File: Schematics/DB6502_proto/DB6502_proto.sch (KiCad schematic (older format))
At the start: 27 parts, among them SW1 Reset, U1 DS1813, U10 62256, U11 74AC138, U12 28C256, U13 22V10C, U2 74AC32, U3 74HC21, U4 65C02S, U5 74AC74, U6 74HC74, U7 74AC04, U8 62256, U9 74AC08, X1 14MHz

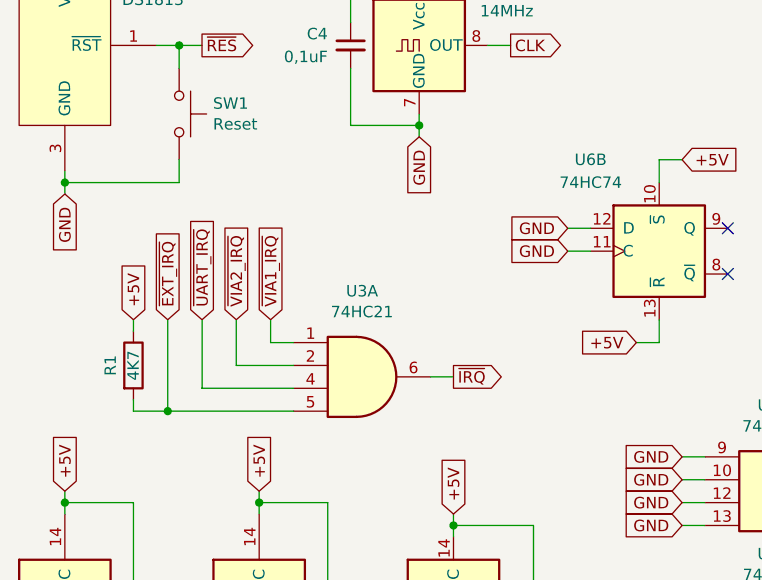
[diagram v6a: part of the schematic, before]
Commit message: Added missing pull-up on UART IRQ line
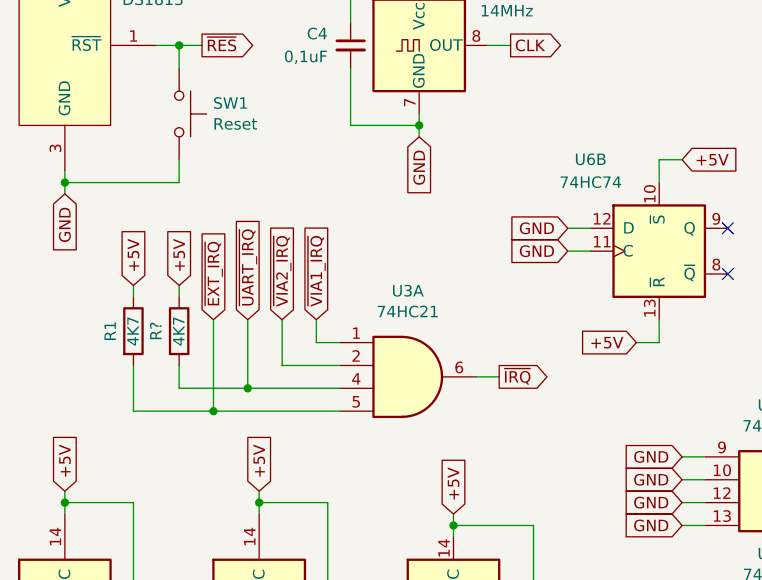
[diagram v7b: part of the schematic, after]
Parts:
- added R?: 4K7, symbol Device:R
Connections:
- net +5V: now also R?.1
- net ~UART_IRQ: now also R?.2
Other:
- moved on the sheet: R1, U3A
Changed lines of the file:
@@
 L 74xx:74LS21 U3
 U 1 1 5FB20233
-P 2150 5800
-F 0 "U3" H 2150 6175 50  0000 C CNN
-F 1 "74HC21" H 2150 6084 50  0000 C CNN
-F 2 "" H 2150 5800 50  0001 C CNN
-F 3 "http://www.ti.com/lit/gpn/sn74LS21" H 2150 5800 50  0001 C CNN
-	1    2150 5800
+P 2350 5800
+F 0 "U3" H 2350 6175 50  0000 C CNN
+F 1 "74HC21" H 2350 6084 50  0000 C CNN
+F 2 "" H 2350 5800 50  0001 C CNN
+F 3 "http://www.ti.com/lit/gpn/sn74LS21" H 2350 5800 50  0001 C CNN
+	1    2350 5800
 	1    0    0    -1
 $EndComp
@@
 Wire Wire Line
 	1700 7450 1700 7400
-Text GLabel 1750 5550 1    50   Input ~ 0
+Text GLabel 1950 5550 1    50   Input ~ 0
 ~VIA1_IRQ
 Wire Wire Line
-	1750 5550 1750 5650
-Wire Wire Line
-	1750 5650 1850 5650
-Text GLabel 1600 5550 1    50   Input ~ 0
+	1950 5550 1950 5650
+Wire Wire Line
+	1950 5650 2050 5650
+Text GLabel 1800 5550 1    50   Input ~ 0
 ~VIA2_IRQ
-Text GLabel 1450 5550 1    50   Input ~ 0
+Text GLabel 1650 5550 1    50   Input ~ 0
 ~UART_IRQ
-Text GLabel 1300 5550 1    50   Input ~ 0
+Text GLabel 1500 5550 1    50   Input ~ 0
 ~EXT_IRQ
-Text GLabel 2550 5800 2    50   Output ~ 0
+Text GLabel 2750 5800 2    50   Output ~ 0
 ~IRQ
 Wire Wire Line
-	2450 5800 2550 5800
-Wire Wire Line
-	1600 5550 1600 5750
-Wire Wire Line
-	1600 5750 1850 5750
-Wire Wire Line
-	1450 5550 1450 5850
-Wire Wire Line
-	1450 5850 1850 5850
-Wire Wire Line
-	1300 5550 1300 5950
-Wire Wire Line
-	1300 5950 1850 5950
+	2650 5800 2750 5800
+Wire Wire Line
+	1800 5550 1800 5750
+Wire Wire Line
+	1800 5750 2050 5750
+Wire Wire Line
+	1650 5550 1650 5850
+Wire Wire Line
+	1650 5850 2050 5850
+Wire Wire Line
+	1500 5550 1500 5950
+Wire Wire Line
+	1500 5950 2050 5950
 $Comp
 L Device:R R1
 U 1 1 5FC6DB04
-P 1150 5750
-F 0 "R1" V 1050 5750 50  0000 C CNN
-F 1 "4K7" V 1150 5750 50  0000 C CNN
-F 2 "" V 1080 5750 50  0001 C CNN
-F 3 "~" H 1150 5750 50  0001 C CNN
-	1    1150 5750
-	1    0    0    -1
-$EndComp
-Text GLabel 1150 5550 1    50   Input ~ 0
-+5V
-Wire Wire Line
-	1150 5550 1150 5600
-Wire Wire Line
-	1150 5900 1150 5950
-Wire Wire Line
-	1150 5950 1300 5950
-Connection ~ 1300 5950
+P 1150 5600
+F 0 "R1" V 1050 5600 50  0000 C CNN
+F 1 "4K7" V 1150 5600 50  0000 C CNN
+F 2 "" V 1080 5600 50  0001 C CNN
+F 3 "~" H 1150 5600 50  0001 C CNN
+	1    1150 5600
+	1    0    0    -1
+$EndComp
+Text GLabel 1150 5400 1    50   Input ~ 0
++5V
+Wire Wire Line
+	1150 5400 1150 5450
+Wire Wire Line
+	1150 5950 1500 5950
+Connection ~ 1500 5950
 Text GLabel 3550 6150 0    50   Input ~ 0
 GND
@@
 Wire Wire Line
 	3450 4850 3550 4850
+$Comp
+L Device:R R?
+U 1 1 6011A69F
+P 1350 5600
+F 0 "R?" V 1250 5600 50  0000 C CNN
+F 1 "4K7" V 1350 5600 50  0000 C CNN
+F 2 "" V 1280 5600 50  0001 C CNN
+F 3 "~" H 1350 5600 50  0001 C CNN
+	1    1350 5600
+	1    0    0    -1
+$EndComp
+Text GLabel 1350 5400 1    50   Input ~ 0
++5V
+Wire Wire Line
+	1350 5400 1350 5450
+Wire Wire Line
+	1150 5750 1150 5950
+Wire Wire Line
+	1350 5750 1350 5850
+Wire Wire Line
+	1350 5850 1650 5850
 Wire Bus Line
 	6500 3750 6500 3950
@@
 Wire Bus Line
 	1600 2150 1600 3400
+Connection ~ 1650 5850
 $EndSCHEMATC

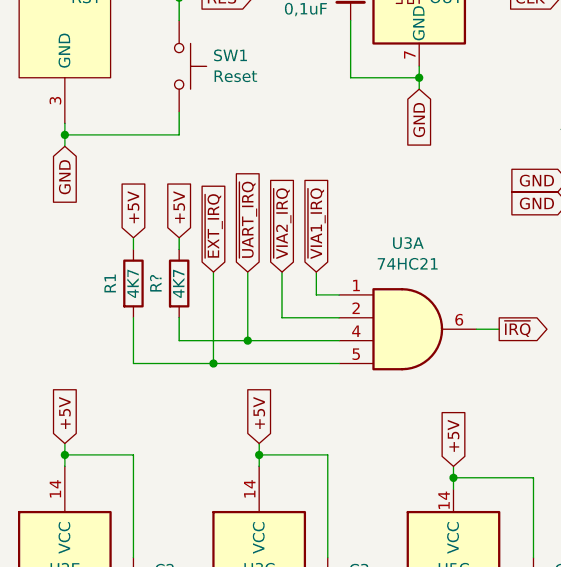
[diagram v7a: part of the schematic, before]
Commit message: Added jumpers for serial source selection
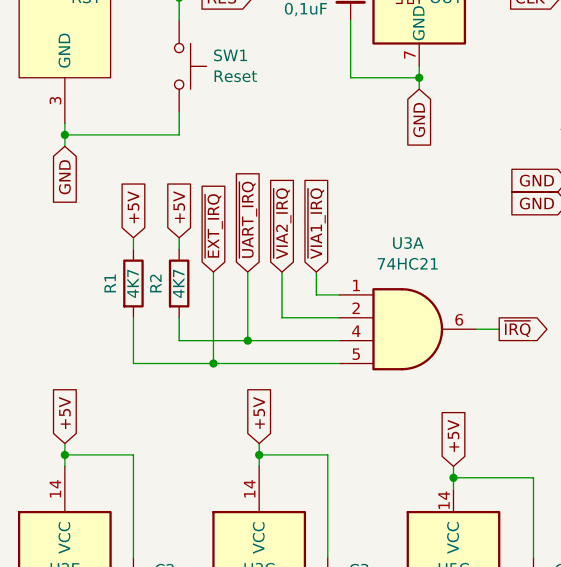
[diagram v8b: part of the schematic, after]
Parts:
- gave numbers to parts that had none: 1
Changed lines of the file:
@@
 	3450 4850 3550 4850
 $Comp
-L Device:R R?
+L Device:R R2
 U 1 1 6011A69F
 P 1350 5600
-F 0 "R?" V 1250 5600 50  0000 C CNN
+F 0 "R2" V 1250 5600 50  0000 C CNN
 F 1 "4K7" V 1350 5600 50  0000 C CNN
 F 2 "" V 1280 5600 50  0001 C CNN
@@
 Wire Wire Line
 	1350 5850 1650 5850
+Connection ~ 1650 5850
 Wire Bus Line
 	6500 3750 6500 3950
@@
 Wire Bus Line
 	1600 2150 1600 3400
-Connection ~ 1650 5850
 $EndSCHEMATC
